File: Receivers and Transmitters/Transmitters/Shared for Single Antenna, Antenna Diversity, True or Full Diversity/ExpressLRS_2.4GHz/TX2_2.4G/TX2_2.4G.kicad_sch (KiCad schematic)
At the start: 11 parts, among them J1 Conn_01x05_Socket, J2 Conn_01x03_Socket, J3 Conn_01x04_Socket, U1 TPS7A4701xRGW, U2 ESP32-WROOM-32, U3 E28-2G4M27S

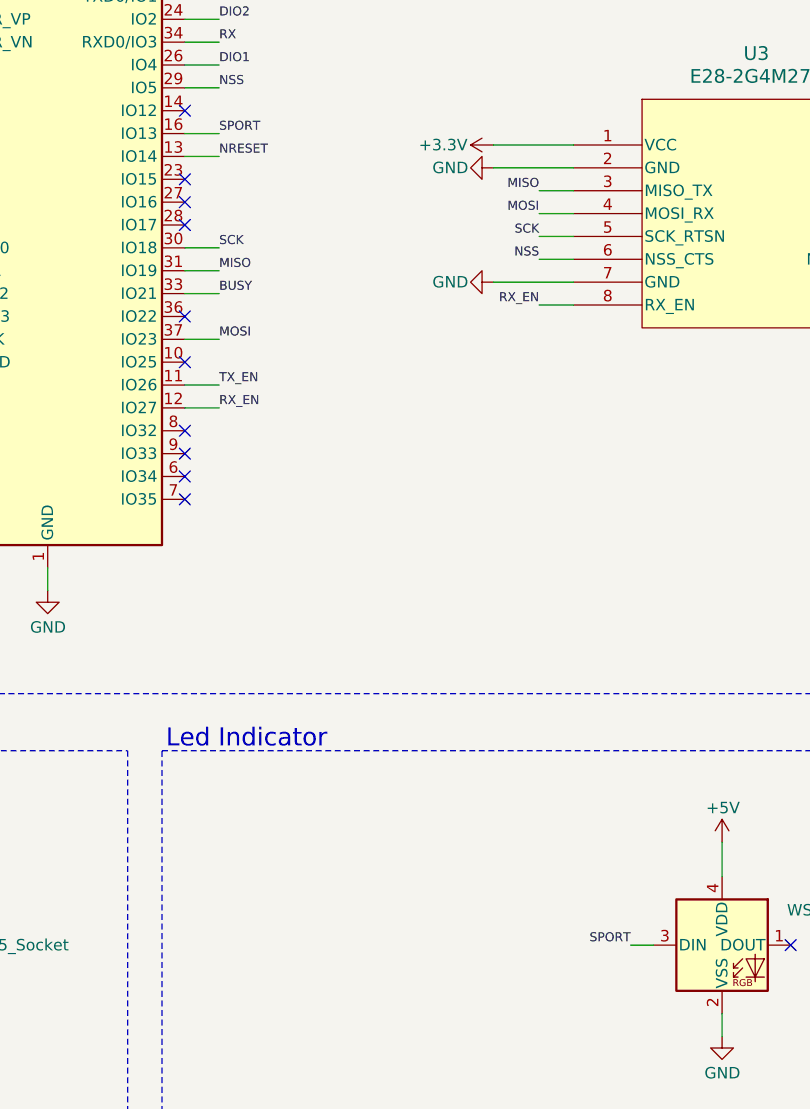
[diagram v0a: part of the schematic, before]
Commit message: Fixed incorrect LED RGB connection to ESP32 on TX2_2.4G and TX3_2.4G schematics and PCBs
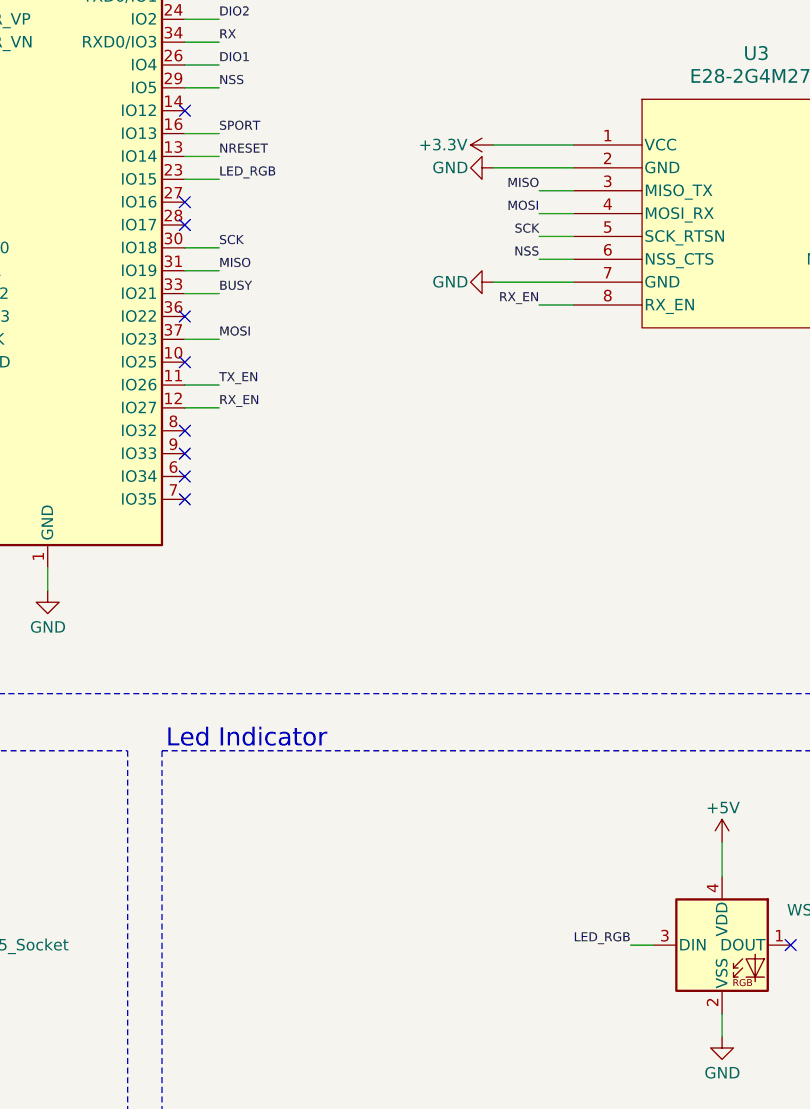
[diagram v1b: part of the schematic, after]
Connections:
- net SPORT: no longer D1.3 (DIN)
- net LED_RGB: now reaches U2.23 (IO15)
- net LED_RGB: now also D1.3 (DIN)
- no-connect marks 25 -> 24
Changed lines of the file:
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@@
-	)
-	(no_connect
-		(at 157.48 57.15)
 	)
 	(no_connect
@@
 	(wire
 		(pts
+			(xy 157.48 57.15) (xy 161.29 57.15)
+		)
+		(stroke
+			(width 0)
+			(type default)
+		)
+	)
+	(wire
+		(pts
 			(xy 86.36 55.88) (xy 86.36 57.15)
 		)
@@
 		)
 	)
+	(label "LED_RGB"
+		(at 161.29 57.15 0)
+		(effects
+			(font
+				(size 1 1)
+			)
+			(justify left bottom)
+		)
+	)
 	(label "BUSY"
 		(at 243.84 63.5 0)
@@
 		)
 	)
-	(label "SPORT"
+	(label "LED_RGB"
 		(at 207.01 142.24 180)
 		(effects
